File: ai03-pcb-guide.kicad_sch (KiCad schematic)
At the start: 14 parts

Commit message: Annotate schematic and assign footprints.
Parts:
- added D1, D2, D3, D4: SOD-123, Diode_SMD:D_SOD-123, symbol Device:D_Small
- added F1: 500mA, Fuse:Fuse_1206_3216Metric, symbol Device:Polyfuse_Small
- added MX1, MX2, MX3, MX4: MX-NoLED, MX_Alps_Hybrid:MX-1U-NoLED, symbol MX_Alps_Hybrid:MX-NoLED
- added USB1: Molex-0548190589, random-keyboard-parts:Molex-0548190589, symbol random-keyboard-parts:Molex-0548190589
- C1, C2, C3, C4, C5, C6, C7: renamed from C?; footprint (none) -> Capacitor_SMD:C_0805_2012Metric
- R1, R2, R3, R4: renamed from R?; footprint (none) -> Resistor_SMD:R_0805_2012Metric
- SW1: renamed from SW?; footprint (none) -> random-keyboard-parts:SKQG-1155865
- Y1: renamed from Y?; footprint (none) -> Crystal:Crystal_SMD_3225-4Pin_3.2x2.5mm
- gave numbers to parts that had none: 1
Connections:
- net +5V: now also F1.2
- net D+: now also USB1.3 (D+)
- net D-: now also USB1.4 (D-)
- net GND: now also USB1.1 (GND)
- new net: D2.2 (A), MX2.2 (ROW)
- new net: D1.2 (A), MX1.2 (ROW)
- new net: D4.2 (A), MX4.2 (ROW)
- new net: D3.2 (A), MX3.2 (ROW)
- new net COL0: MX1.1 (COL), MX3.1 (COL)
- new net COL1: MX2.1 (COL), MX4.1 (COL)
- new net ROW0: D1.1 (K), D2.1 (K)
- new net ROW1: D3.1 (K), D4.1 (K)
- new net VCC: F1.1, USB1.5 (VBUS)
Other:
- moved on the sheet: C1, C2, C3, C4, C5, C6, C7, R1, R2, R3, R4, SW1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

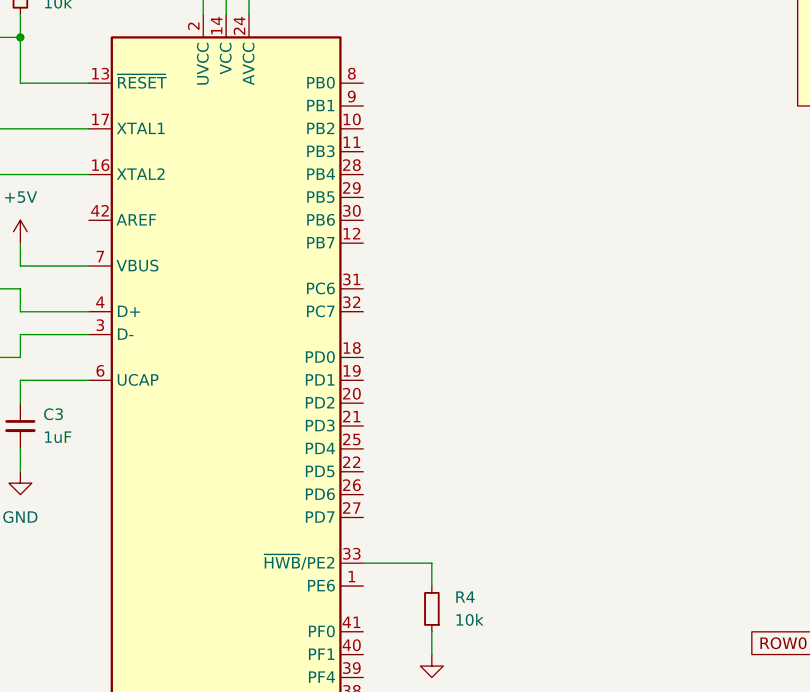
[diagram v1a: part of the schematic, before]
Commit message: Create and route PCB.
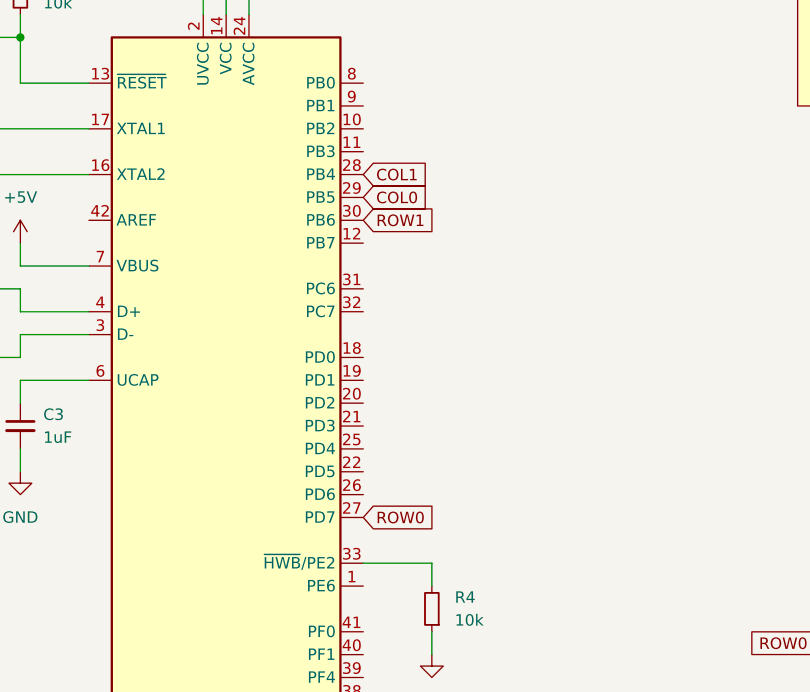
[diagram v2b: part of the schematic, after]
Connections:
- net COL0: now also U1.29 (PB5)
- net COL1: now also U1.28 (PB4)
- net ROW0: now also U1.27 (PD7)
- net ROW1: now also U1.30 (PB6)
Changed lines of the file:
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@@
+    )
+  )
+  (global_label "COL1" (shape input) (at 118.11 77.47 0) (fields_autoplaced)
+    (effects (font (size 1.27 1.27)) (justify left))
+    (property "Intersheet References" "${INTERSHEET_REFS}" (id 0) (at 125.3612 77.3906 0)
+      (effects (font (size 1.27 1.27)) (justify left) hide)
     )
   )
@@
       (effects (font (size 1.27 1.27)) (justify left) hide)
     )
+  )
+  (global_label "ROW0" (shape input) (at 118.11 115.57 0) (fields_autoplaced)
+    (effects (font (size 1.27 1.27)) (justify left))
+    (property "Intersheet References" "${INTERSHEET_REFS}" (id 0) (at 125.7845 115.6494 0)
+      (effects (font (size 1.27 1.27)) (justify left) hide)
+    )
+  )
+  (global_label "COL0" (shape input) (at 118.11 80.01 0) (fields_autoplaced)
+    (effects (font (size 1.27 1.27)) (justify left))
+    (property "Intersheet References" "${INTERSHEET_REFS}" (id 0) (at 125.3612 79.9306 0)
+      (effects (font (size 1.27 1.27)) (justify left) hide)
+    )
+  )
+  (global_label "ROW1" (shape input) (at 118.11 82.55 0) (fields_autoplaced)
+    (effects (font (size 1.27 1.27)) (justify left))
+    (property "Intersheet References" "${INTERSHEET_REFS}" (id 0) (at 125.7845 82.6294 0)
+      (effects (font (size 1.27 1.27)) (justify left) hide)
+    )
